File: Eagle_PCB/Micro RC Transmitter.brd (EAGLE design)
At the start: 81.3 x 58.4 mm, 34 parts, among them IC1 NRF24L01+, Q1 BC337-25, U1 JOYSTICKPTH, U2 JOYSTICKPTH, U3 ARDUINO_PRO_MINI, U4 0.96"_I2C_OLED2

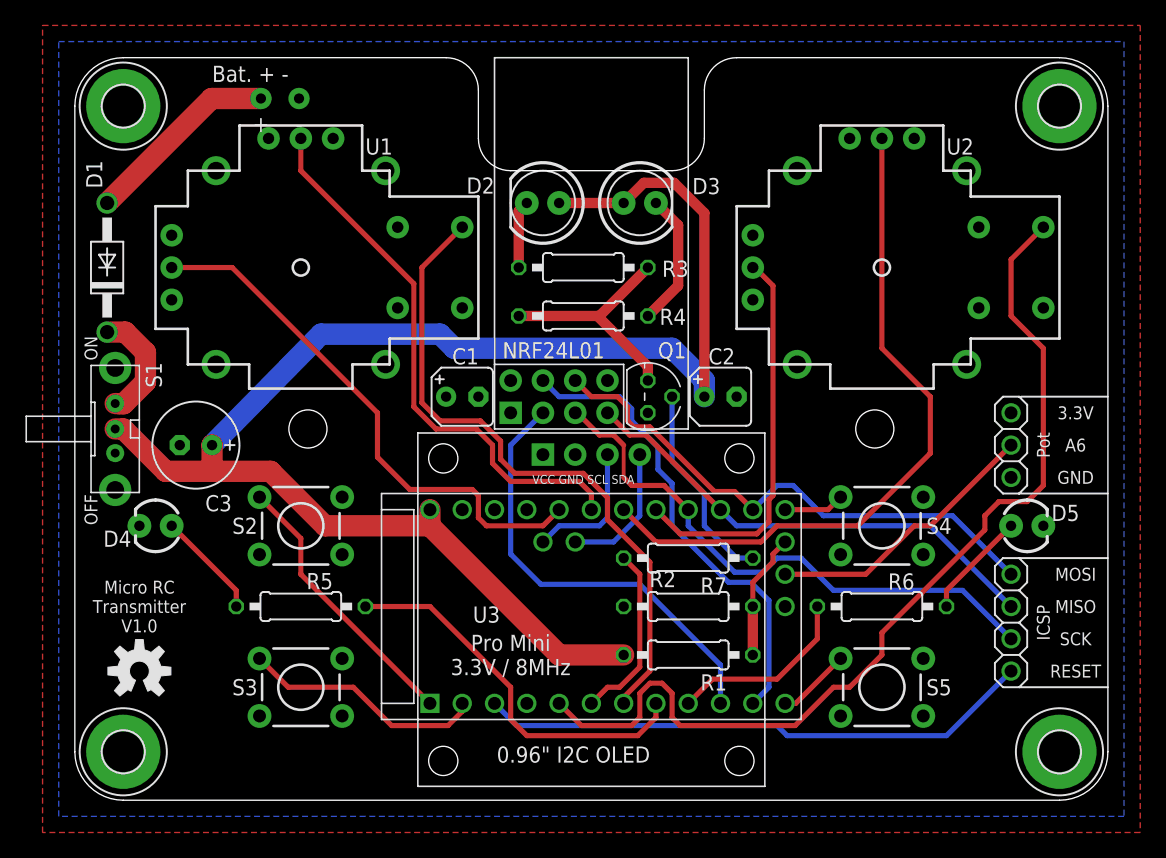
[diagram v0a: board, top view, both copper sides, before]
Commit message: New board revision 1.2
separate voltage regulator for NRF24L01 radio transmitter. Allows to use a a model with power amplifier.
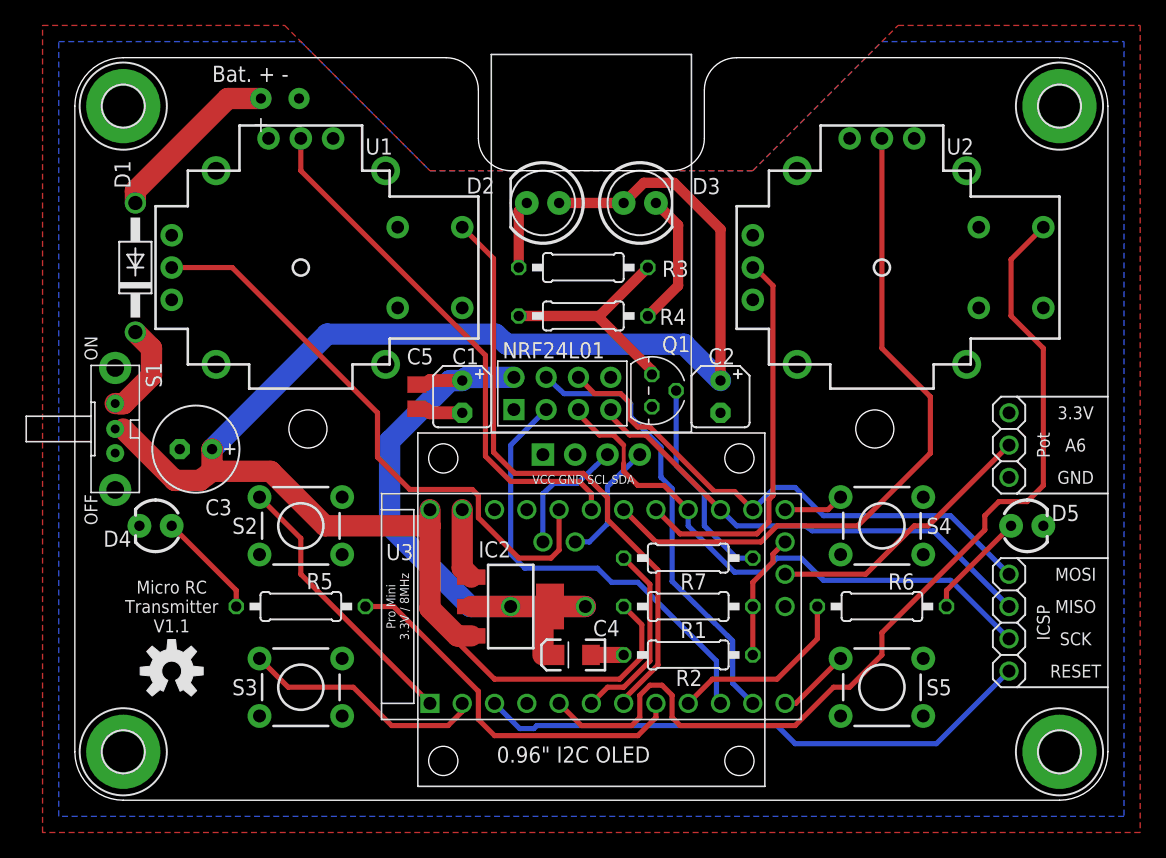
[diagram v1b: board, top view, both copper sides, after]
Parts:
- added C4: 10uF, SparkFun-Capacitors:EIA3216
- added C5: 100nF, rcl:C0805
- added IC2: 1117-3.3, lm1117:SOT223
- moved R1 3.81 mm to (48.3, 15.2)
- moved R2 3.81 mm to (48.3, 11.4)
- moved LOGO1 2.54 mm to (7.62, 10.2)
- moved D1 2.22 mm to (4.76, 41.9)
- moved Q1 0.57 mm to (45.4, 32.2)
- moved IC1 0.36 mm to (33.3, 29.5)
- moved C3 0.32 mm to (9.53, 27.6)
- moved JP1 0.16 mm to (73.5, 14.0)
- moved JP2 0.16 mm to (73.5, 27.9)
- turned C1 to 270 degrees
- turned C2 to 270 degrees
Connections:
- removed net VCC: C2.+, C3.+, D2.A, D3.A, R1.2, S1.2, U3.24
- new net N$9: C1.+, C4.A, C5.1, IC1.2, IC2.2, IC2.TAB
- new net RAW: C2.+, C3.+, D2.A, D3.A, IC2.3, R1.2, S1.2, U3.24
- net +3V3: no longer C1.+, IC1.2
- net GND: now also C4.C, C5.2, IC2.1
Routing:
- net RAW: track 0.00 -> 138.4 mm
- net VCC: track 123.4 -> 0.00 mm
- net N$9: track 0.00 -> 54.6 mm, vias 0 -> 2
- net GND: track 0.00 -> 11.9 mm
- net 4: track 52.1 -> 48.1 mm
- net A3: track 42.5 -> 46.5 mm
- net 8: track 37.1 -> 35.1 mm
- net A2: track 43.7 -> 41.8 mm
- net N$7: track 15.5 -> 13.8 mm
- net N$8: track 9.10 -> 7.74 mm
- net A4: track 10.7 -> 9.64 mm
- net 3: track 14.1 -> 14.9 mm
- net A5: track 10.8 -> 10.1 mm
- net RESET: track 43.8 -> 44.4 mm
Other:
- board text added: "Micro RC Transmitter V1.1"
- board text removed: "Micro RC Transmitter V1.0"

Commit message: LED resistor values increased
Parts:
- R3, R5, R6: value 100R -> 150R
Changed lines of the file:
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@@
 <attribute name="PROD_ID" value="DIO-08794" x="74.93" y="21.59" size="1.778" layer="27" display="off"/>
 </element>
-<element name="R5" library="rcl" package="0207/10" value="100R" x="17.78" y="15.24" smashed="yes">
+<element name="R5" library="rcl" package="0207/10" value="150R" x="17.78" y="15.24" smashed="yes">
 <attribute name="NAME" x="18.2245" y="16.60525" size="1.27" layer="25" ratio="10"/>
 <attribute name="VALUE" x="15.5194" y="14.605" size="1.27" layer="27" ratio="10"/>
 </element>
-<element name="R6" library="rcl" package="0207/10" value="100R" x="63.5" y="15.24" smashed="yes" rot="R180">
+<element name="R6" library="rcl" package="0207/10" value="150R" x="63.5" y="15.24" smashed="yes" rot="R180">
 <attribute name="NAME" x="66.07175" y="17.8435" size="1.27" layer="25" ratio="10" rot="R180"/>
 <attribute name="VALUE" x="65.7606" y="15.875" size="1.27" layer="27" ratio="10" rot="R180"/>
@@
 <attribute name="NAME" x="4.3815" y="48.133" size="1.27" layer="25" ratio="10" rot="R90"/>
 </element>
-<element name="R3" library="rcl" package="0207/10" value="100R" x="40.005" y="41.91" smashed="yes" rot="R180">
+<element name="R3" library="rcl" package="0207/10" value="150R" x="40.005" y="41.91" smashed="yes" rot="R180">
 <attribute name="NAME" x="48.29175" y="42.44975" size="1.27" layer="25" ratio="10" rot="R180"/>
 <attribute name="VALUE" x="42.2656" y="42.545" size="1.27" layer="27" ratio="10" rot="R180"/>
